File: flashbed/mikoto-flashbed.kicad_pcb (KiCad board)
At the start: 2 copper layers, 50 x 43 mm, 49 parts, among them J1 Conn_01x01, J2 Conn_01x01, J3 Conn_01x01, J4 Conn_01x01, J5 Conn_01x01, J6 Conn_01x01, J7 Conn_01x05, SW1 TVBP06, U1 ProMicro_2

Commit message: update flashbed and add gerbers
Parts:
- removed D10, D11, D12, D13, D14, D15, D16, D17, D18, D19, D2, D20, D3, D4, D5, D6, D7, D8, D9: LED_Small, LED_SMD:LED_1206_3216Metric_Pad1.42x1.75mm_HandSolder
- removed R10, R11, R12, R13, R14, R15, R16, R17, R18, R19, R2, R20, R3, R4, R5, R6, R7, R8, R9: 2.2k, Resistor_SMD:R_0805_2012Metric_Pad1.15x1.40mm_HandSolder
- added J8: Conn_01x01, Connector_PinHeader_2.54mm:PinHeader_1x01_P2.54mm_Vertical, F.Cu at (-14.0, -5.00)
- moved R1 36.5 mm to (-14.0, 8.99), turned to -90 degrees
- moved D1 31.3 mm to (-14.0, 3.50), turned to 90 degrees
- moved SW1 5.70 mm to (13.5, -3.50), turned to -90 degrees
- moved J7 2.50 mm to (-5.08, 20.5)
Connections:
- D1 pad 2: P0.09 -> Net-(D1-Pad2)
- J5 pad 1: EXT_5V -> unconnected-(J5-Pad1)
- J6 pad 1: VBUS -> unconnected-(J6-Pad1)
- U1 pad 1: P0.06 -> unconnected-(U1-Pad1)
- U1 pad 10: P0.31 -> unconnected-(U1-Pad10)
- U1 pad 11: P1.04 -> unconnected-(U1-Pad11)
- U1 pad 12: P1.06 -> unconnected-(U1-Pad12)
- U1 pad 13: P0.09 -> unconnected-(U1-Pad13)
- U1 pad 14: P0.10 -> unconnected-(U1-Pad14)
- U1 pad 15: P1.11 -> unconnected-(U1-Pad15)
- U1 pad 16: P1.13 -> unconnected-(U1-Pad16)
- U1 pad 17: P1.15 -> unconnected-(U1-Pad17)
- U1 pad 18: P0.02 -> unconnected-(U1-Pad18)
- U1 pad 19: P0.25 -> unconnected-(U1-Pad19)
- U1 pad 2: P0.08 -> unconnected-(U1-Pad2)
- U1 pad 20: P0.11 -> unconnected-(U1-Pad20)
- U1 pad 21: EXT_VCC -> unconnected-(U1-Pad21)
- U1 pad 24: VBAT -> unconnected-(U1-Pad24)
- U1 pad 5: P0.17 -> unconnected-(U1-Pad5)
- U1 pad 6: P0.20 -> unconnected-(U1-Pad6)
- U1 pad 7: P0.22 -> unconnected-(U1-Pad7)
- U1 pad 8: P0.24 -> unconnected-(U1-Pad8)
- U1 pad 9: P1.00 -> unconnected-(U1-Pad9)
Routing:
- net GND: track 63.4 -> 5.78 mm, vias 98 -> 47
- net Net-(D1-Pad2): track 0.00 -> 10.4 mm, vias 0 -> 1
- net VBUS: track 5.89 -> 0.00 mm
- net P1.15: track 5.89 -> 0.00 mm
- net P1.13: track 5.89 -> 0.00 mm
- net P1.11: track 5.89 -> 0.00 mm
- net P1.06: track 5.89 -> 0.00 mm
- net P1.04: track 5.89 -> 0.00 mm
- net P1.00: track 5.89 -> 0.00 mm
- net P0.31: track 5.89 -> 0.00 mm
- net P0.25: track 5.89 -> 0.00 mm
- net P0.24: track 5.89 -> 0.00 mm
- net P0.22: track 5.89 -> 0.00 mm
- net P0.20: track 5.89 -> 0.00 mm
- net P0.17: track 5.89 -> 0.00 mm
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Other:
- board size 50 x 43 mm -> 46 x 46 mm
- board text added: "rev 1.3"
- board text removed: "rev 1.0"

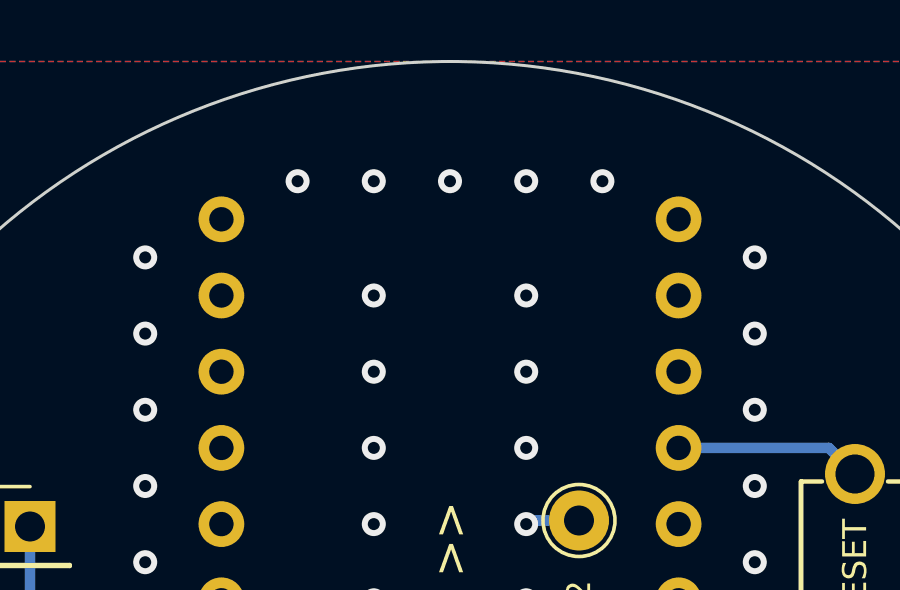
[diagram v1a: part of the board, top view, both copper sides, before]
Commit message: rev 5.11
1. move thermal vias for bq24075 to not be literally under the paste
2. reduce the EP paste for the nrf52 (and place the vias between the
   paste islands)
3. remove all silks for passives because it's ugly
4. fix the incorrect pin labelling (since we switched P0.06 to P0.04)
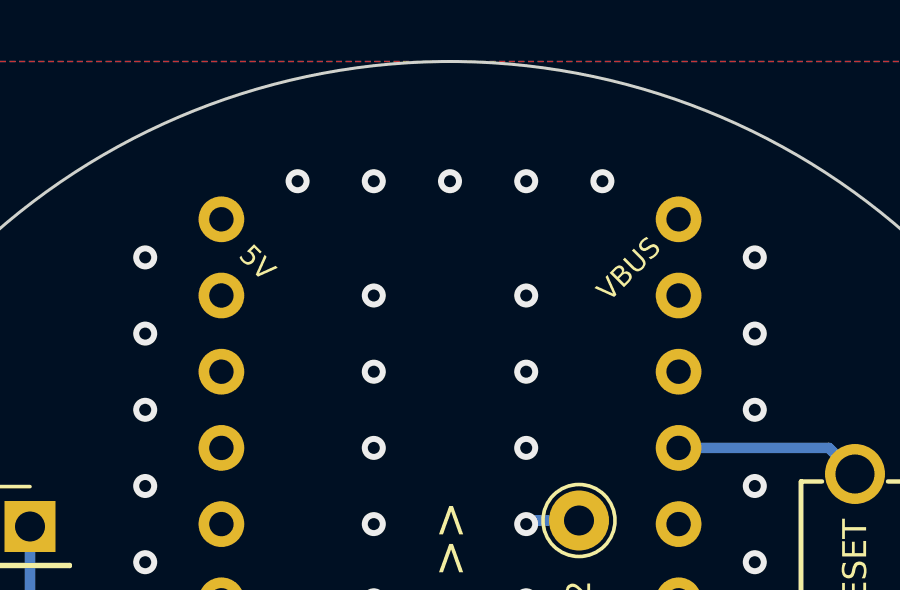
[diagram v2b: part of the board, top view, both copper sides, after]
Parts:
- removed J5, J6: Conn_01x01, footprints:1pin_conn
- U1: value ProMicro_2 -> mikoto-pins; footprint footprints:akami-pins -> footprints:mikoto-pins
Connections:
- U1 pad 22: RESET -> unconnected-(U1-Pad22)
- U1 pad 23: GND -> RESET
- U1 pad 24: unconnected-(U1-Pad24) -> GND
- U1 pad 3: GND -> unconnected-(U1-Pad3)
- U1 pad 5: unconnected-(U1-Pad5) -> GND

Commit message: update flashbed
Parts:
- removed J8: Conn_01x01, Connector_PinHeader_2.54mm:PinHeader_1x01_P2.54mm_Vertical
- added D10: LED_Small, footprints:LED_1206_3216M_Castellated-nosilk, F.Cu at (-17.1, 12.7)
- added D11: LED_Small, footprints:LED_1206_3216M_Castellated-nosilk, F.Cu at (-17.1, 15.2)
- added D12: LED_Small, footprints:LED_1206_3216M_Castellated-nosilk, F.Cu at (17.1, 15.2)
- added D13: LED_Small, footprints:LED_1206_3216M_Castellated-nosilk, F.Cu at (17.1, 12.7)
- added D14: LED_Small, footprints:LED_1206_3216M_Castellated-nosilk, F.Cu at (17.1, 10.2)
- added D15: LED_Small, footprints:LED_1206_3216M_Castellated-nosilk, F.Cu at (17.1, 7.62)
- added D16: LED_Small, footprints:LED_1206_3216M_Castellated-nosilk, F.Cu at (17.1, 5.08)
- added D17: LED_Small, footprints:LED_1206_3216M_Castellated-nosilk, F.Cu at (17.1, 2.54)
- added D18: LED_Small, footprints:LED_1206_3216M_Castellated-nosilk, F.Cu at (17.1, 0.00)
- added D19: LED_Small, footprints:LED_1206_3216M_Castellated-nosilk, F.Cu at (17.1, -2.54)
- added D2: LED_Small, footprints:LED_1206_3216M_Castellated-nosilk, F.Cu at (-17.1, -12.7)
- added D20: LED_Small, footprints:LED_1206_3216M_Castellated-nosilk, F.Cu at (17.1, -5.08)
- added D21: LED_Small, footprints:LED_1206_3216M_Castellated-nosilk, F.Cu at (17.1, -15.2)
- added D3: LED_Small, footprints:LED_1206_3216M_Castellated-nosilk, F.Cu at (-17.1, -10.2)
- added D4: LED_Small, footprints:LED_1206_3216M_Castellated-nosilk, F.Cu at (-17.1, -2.54)
- added D5: LED_Small, footprints:LED_1206_3216M_Castellated-nosilk, F.Cu at (-17.1, 0.00)
- added D6: LED_Small, footprints:LED_1206_3216M_Castellated-nosilk, F.Cu at (-17.1, 2.54)
- added D7: LED_Small, footprints:LED_1206_3216M_Castellated-nosilk, F.Cu at (-17.1, 5.08)
- added D8: LED_Small, footprints:LED_1206_3216M_Castellated-nosilk, F.Cu at (-17.1, 7.62)
- added D9: LED_Small, footprints:LED_1206_3216M_Castellated-nosilk, F.Cu at (-17.1, 10.2)
- added R10: 2.2k, Resistor_SMD:R_0805_2012Metric_Pad1.15x1.40mm_HandSolder, F.Cu at (-12.1, 12.7)
- added R11: 2.2k, Resistor_SMD:R_0805_2012Metric_Pad1.15x1.40mm_HandSolder, F.Cu at (-12.1, 15.2)
- added R12: 2.2k, Resistor_SMD:R_0805_2012Metric_Pad1.15x1.40mm_HandSolder, F.Cu at (12.1, 15.2)
- added R13: 2.2k, Resistor_SMD:R_0805_2012Metric_Pad1.15x1.40mm_HandSolder, F.Cu at (12.1, 12.7)
- added R14: 2.2k, Resistor_SMD:R_0805_2012Metric_Pad1.15x1.40mm_HandSolder, F.Cu at (12.1, 10.2)
- added R15: 2.2k, Resistor_SMD:R_0805_2012Metric_Pad1.15x1.40mm_HandSolder, F.Cu at (12.1, 7.62)
- added R16: 2.2k, Resistor_SMD:R_0805_2012Metric_Pad1.15x1.40mm_HandSolder, F.Cu at (12.1, 5.08)
- added R17: 2.2k, Resistor_SMD:R_0805_2012Metric_Pad1.15x1.40mm_HandSolder, F.Cu at (12.1, 2.54)
- added R18: 2.2k, Resistor_SMD:R_0805_2012Metric_Pad1.15x1.40mm_HandSolder, F.Cu at (12.1, 0.00)
- added R19: 2.2k, Resistor_SMD:R_0805_2012Metric_Pad1.15x1.40mm_HandSolder, F.Cu at (12.1, -2.54)
- added R2: 2.2k, Resistor_SMD:R_0805_2012Metric_Pad1.15x1.40mm_HandSolder, F.Cu at (-12.1, -12.7)
- added R20: 2.2k, Resistor_SMD:R_0805_2012Metric_Pad1.15x1.40mm_HandSolder, F.Cu at (12.1, -5.08)
- added R21: 2.2k, Resistor_SMD:R_0805_2012Metric_Pad1.15x1.40mm_HandSolder, F.Cu at (12.1, -15.2)
- added R3: 2.2k, Resistor_SMD:R_0805_2012Metric_Pad1.15x1.40mm_HandSolder, F.Cu at (-12.1, -10.2)
- added R4: 2.2k, Resistor_SMD:R_0805_2012Metric_Pad1.15x1.40mm_HandSolder, F.Cu at (-12.1, -2.54)
- added R5: 2.2k, Resistor_SMD:R_0805_2012Metric_Pad1.15x1.40mm_HandSolder, F.Cu at (-12.1, 0.00)
- added R6: 2.2k, Resistor_SMD:R_0805_2012Metric_Pad1.15x1.40mm_HandSolder, F.Cu at (-12.1, 2.54)
- added R7: 2.2k, Resistor_SMD:R_0805_2012Metric_Pad1.15x1.40mm_HandSolder, F.Cu at (-12.1, 5.08)
- added R8: 2.2k, Resistor_SMD:R_0805_2012Metric_Pad1.15x1.40mm_HandSolder, F.Cu at (-12.1, 7.62)
- added R9: 2.2k, Resistor_SMD:R_0805_2012Metric_Pad1.15x1.40mm_HandSolder, F.Cu at (-12.1, 10.2)
- D1: footprint LED_SMD:LED_1206_3216Metric_Pad1.42x1.75mm_HandSolder -> footprints:LED_1206_3216M_Castellated-nosilk
- U1: footprint footprints:mikoto-pins -> footprints:mikoto-pins-bigger-holes
- moved R1 24.3 mm to (-12.1, -15.2), turned to 180 degrees
- moved D1 19.0 mm to (-17.1, -15.2), turned to 0 degrees
- moved J2 9.23 mm to (-4.50, -8.00)
- moved SW1 6.88 mm to (15.2, -10.2), turned to 0 degrees
- moved J4 1.33 mm to (-4.50, 5.50)
- moved J1 0.61 mm to (-4.50, 9.50)
- moved J3 0.60 mm to (-1.50, 9.50)
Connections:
- D1 pad 1: Net-(D1-Pad1) -> GND
- R1 pad 1: Net-(D1-Pad1) -> EXT_5V
- R1 pad 2: GND -> Net-(D1-Pad2)
- U1 pad 1: unconnected-(U1-Pad1) -> EXT_5V
- U1 pad 10: unconnected-(U1-Pad10) -> P1.00
- U1 pad 11: unconnected-(U1-Pad11) -> P1.02
- U1 pad 12: unconnected-(U1-Pad12) -> P1.04
- U1 pad 13: unconnected-(U1-Pad13) -> P1.06
- U1 pad 14: unconnected-(U1-Pad14) -> P0.09
- U1 pad 15: unconnected-(U1-Pad15) -> P0.10
- U1 pad 16: unconnected-(U1-Pad16) -> P1.11
- U1 pad 17: unconnected-(U1-Pad17) -> P0.02
- U1 pad 18: unconnected-(U1-Pad18) -> P0.29
- U1 pad 19: unconnected-(U1-Pad19) -> P0.31
- U1 pad 2: unconnected-(U1-Pad2) -> P0.08
- U1 pad 20: unconnected-(U1-Pad20) -> P0.25
- U1 pad 21: unconnected-(U1-Pad21) -> P0.11
- U1 pad 22: unconnected-(U1-Pad22) -> EXT_VCC
- U1 pad 25: unconnected-(U1-Pad25) -> VBAT
- U1 pad 26: unconnected-(U1-Pad26) -> VBUS
- U1 pad 3: unconnected-(U1-Pad3) -> P0.04
- U1 pad 6: unconnected-(U1-Pad6) -> P0.17
- U1 pad 7: unconnected-(U1-Pad7) -> P0.20
- U1 pad 8: unconnected-(U1-Pad8) -> P0.22
- U1 pad 9: unconnected-(U1-Pad9) -> P0.24
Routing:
- net GND: track 5.78 -> 40.8 mm, vias 47 -> 69
- net Net-(D1-Pad1): track 8.24 -> 0.00 mm, vias 2 -> 0
- net Net-(D1-Pad2): track 10.4 -> 2.57 mm, vias 1 -> 0
- net VBUS: track 0.00 -> 3.42 mm
- net P1.11: track 0.00 -> 3.42 mm
- net P1.06: track 0.00 -> 3.42 mm
- net P1.04: track 0.00 -> 3.42 mm
- net P1.02: track 0.00 -> 3.42 mm
- net P1.00: track 0.00 -> 3.42 mm
- net P0.31: track 0.00 -> 3.42 mm
- net P0.29: track 0.00 -> 3.42 mm
- net P0.25: track 0.00 -> 3.42 mm
- net P0.24: track 0.00 -> 3.42 mm
- net P0.22: track 0.00 -> 3.42 mm
- net P0.20: track 0.00 -> 3.42 mm
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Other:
- board size 46 x 46 mm -> 54 x 41.5 mm
- board text added: "E_5V"
- board text added: "E_VCC"
- board text added: "P0.02"
- board text added: "P0.04"
- board text added: "P0.08"
- board text added: "P0.09"
- board text added: "P0.10"
- board text added: "P0.11"
- board text added: "P0.17"
- board text added: "P0.20"
- board text added: "P0.22"
- board text added: "P0.24"
- board text added: "P0.25"
- board text added: "P0.29"
- board text added: "P0.31"
- board text added: "P1.00"
- board text added: "P1.02"
- board text added: "P1.04"
- board text added: "P1.06"
- board text added: "P1.11"
- board text added: "VBUS"
- board text added: "components up"
- board text added: "front >"
- board text added: "rev 2.1"
- board text removed: "rev 1.3"
- board text removed: "this way up >>"

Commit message: some nonsense with the flashbed
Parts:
- added R22: R_Small, Resistor_SMD:R_0201_0603Metric, F.Cu at (-2.00, -14.0)
- added R23: R_Small, Resistor_SMD:R_0201_0603Metric, F.Cu at (-2.00, -12.0)
- added R24: R_Small, Resistor_SMD:R_0201_0603Metric, F.Cu at (-2.00, -10.0)
- added R25: R_Small, Resistor_SMD:R_0201_0603Metric, F.Cu at (-2.00, -8.00)
- added R26: R_Small, Resistor_SMD:R_0201_0603Metric, F.Cu at (-2.00, -6.00)
- added R27: R_Small, Resistor_SMD:R_0201_0603Metric, F.Cu at (-2.00, -4.00)
- added R28: R_Small, Resistor_SMD:R_0201_0603Metric, F.Cu at (-2.00, -2.00)
- added R29: R_Small, Resistor_SMD:R_0201_0603Metric, F.Cu at (-2.00, 0.00)
- added TP1: TestPoint, footprints:TestPoint_Pad_D1.0mm-nosilk, F.Cu at (2.00, -14.0)
- added TP2: TestPoint, footprints:TestPoint_Pad_D1.0mm-nosilk, F.Cu at (2.00, -12.0)
- added TP3: TestPoint, footprints:TestPoint_Pad_D1.0mm-nosilk, F.Cu at (2.00, -10.0)
- added TP4: TestPoint, footprints:TestPoint_Pad_D1.0mm-nosilk, F.Cu at (2.00, -8.00)
- added TP5: TestPoint, footprints:TestPoint_Pad_D1.0mm-nosilk, F.Cu at (2.00, -6.00)
- added TP6: TestPoint, footprints:TestPoint_Pad_D1.0mm-nosilk, F.Cu at (2.00, -4.00)
- added TP7: TestPoint, footprints:TestPoint_Pad_D1.0mm-nosilk, F.Cu at (2.00, -2.00)
- added TP8: TestPoint, footprints:TestPoint_Pad_D1.0mm-nosilk, F.Cu at (2.00, 0.00)
- J7: footprint Connector_PinHeader_2.54mm:PinHeader_1x05_P2.54mm_Vertical -> Connector_PinHeader_2.54mm:PinHeader_1x05_P2.54mm_Horizontal
- moved J7 10.2 mm to (5.08, 20.5), turned to -90 degrees
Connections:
- J7 pad 1: SWD -> unconnected-(J7-Pad1)
- J7 pad 2: GND -> VDD
- J7 pad 4: VDD -> GND
- J7 pad 5: unconnected-(J7-Pad5) -> SWD
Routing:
- net EXT_5V: track 3.42 -> 13.8 mm
- net Net-(R27-Pad1): track 0.00 -> 5.49 mm
- net Net-(R28-Pad1): track 0.00 -> 5.49 mm
- net Net-(R26-Pad1): track 0.00 -> 5.49 mm
- net Net-(R25-Pad1): track 0.00 -> 5.49 mm
- net Net-(R24-Pad1): track 0.00 -> 5.49 mm
- net Net-(R23-Pad1): track 0.00 -> 5.49 mm
- net Net-(R22-Pad1): track 0.00 -> 5.49 mm

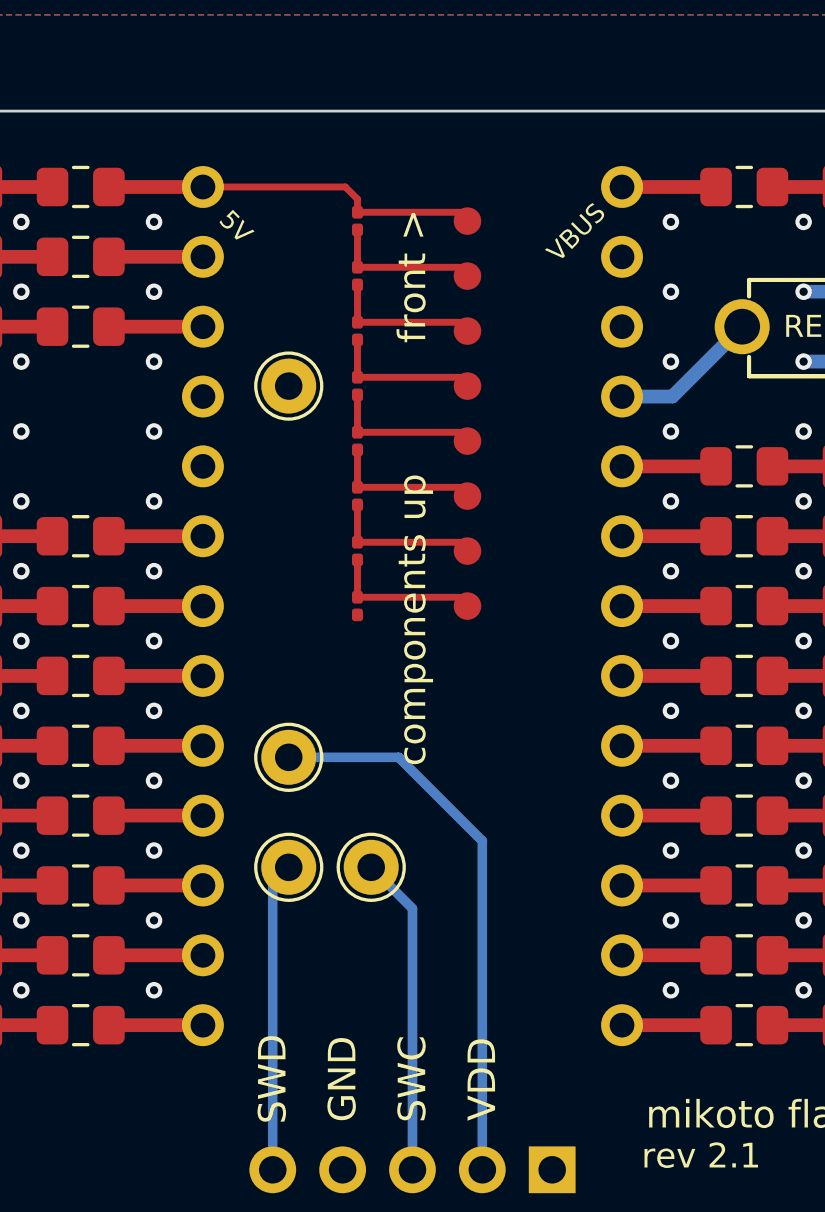
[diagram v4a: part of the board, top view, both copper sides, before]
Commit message: rev 5.14
change LDO pulldown to 2M. tweak routing and other small things.
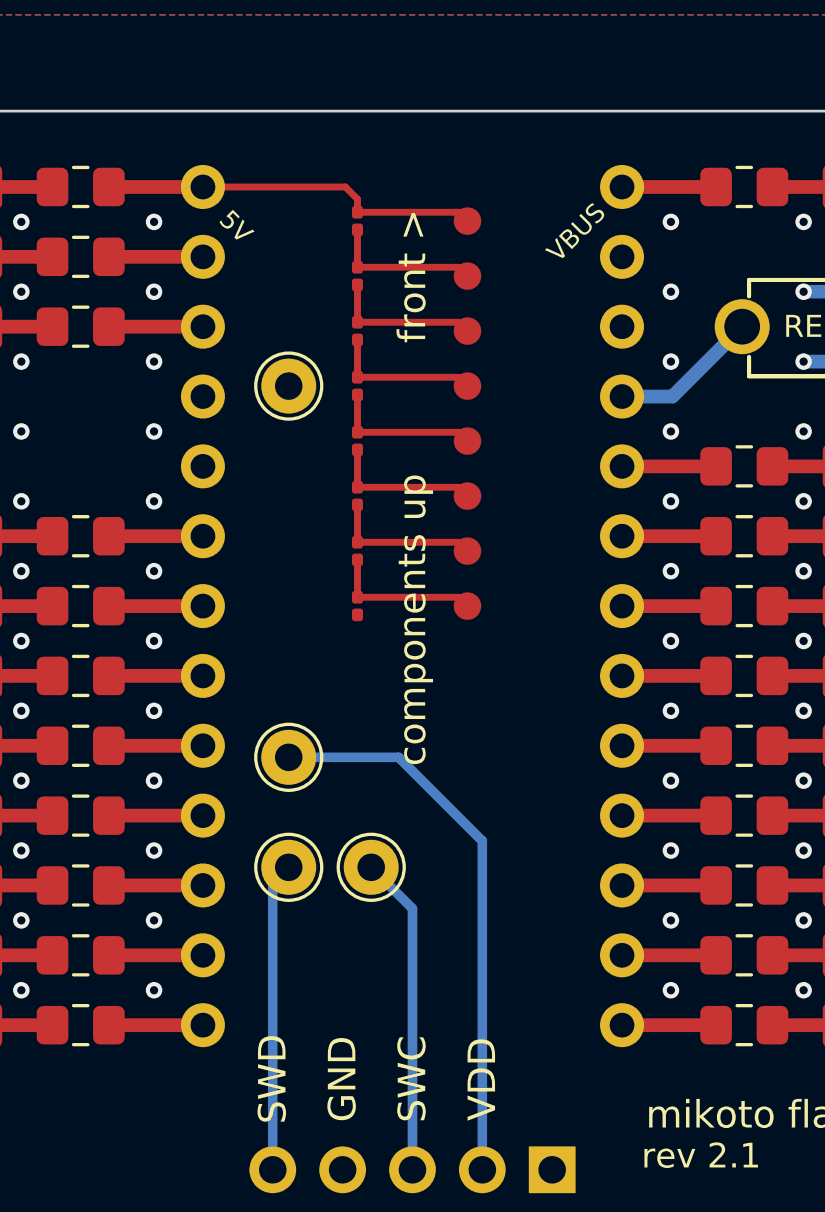
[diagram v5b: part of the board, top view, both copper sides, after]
